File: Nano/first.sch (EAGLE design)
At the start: 17 parts, among them J2 455-1750-1-ND, J3 455-1750-1-ND

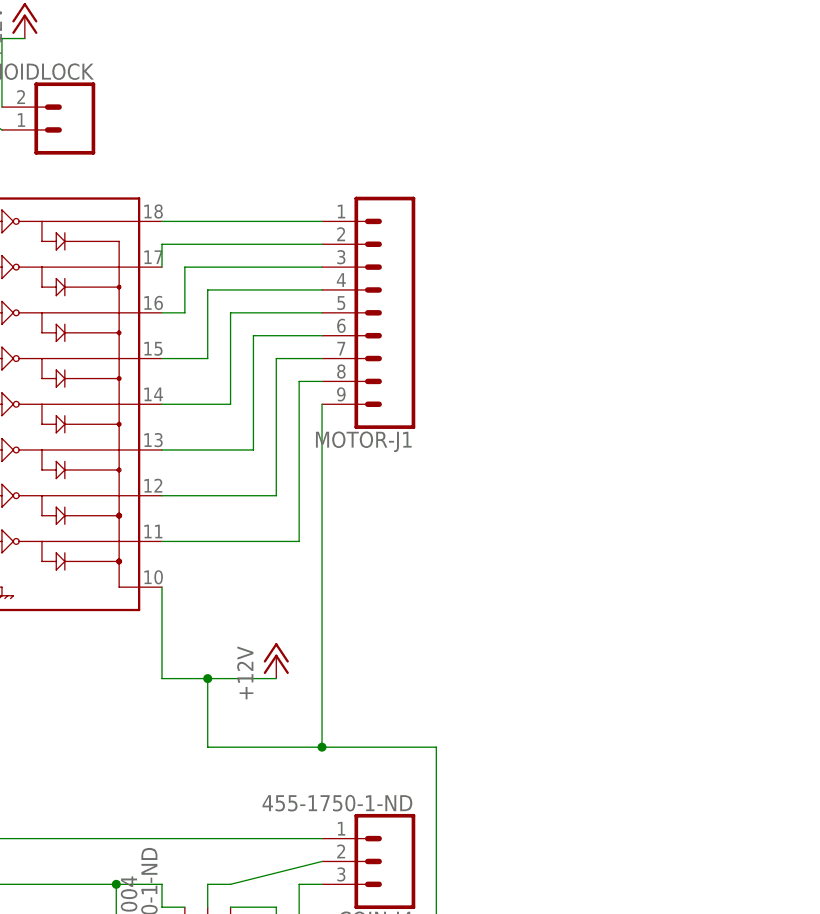
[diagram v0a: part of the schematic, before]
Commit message: Mini board schematic updated (molex conn added, uno mirrored, tracks and via changed)
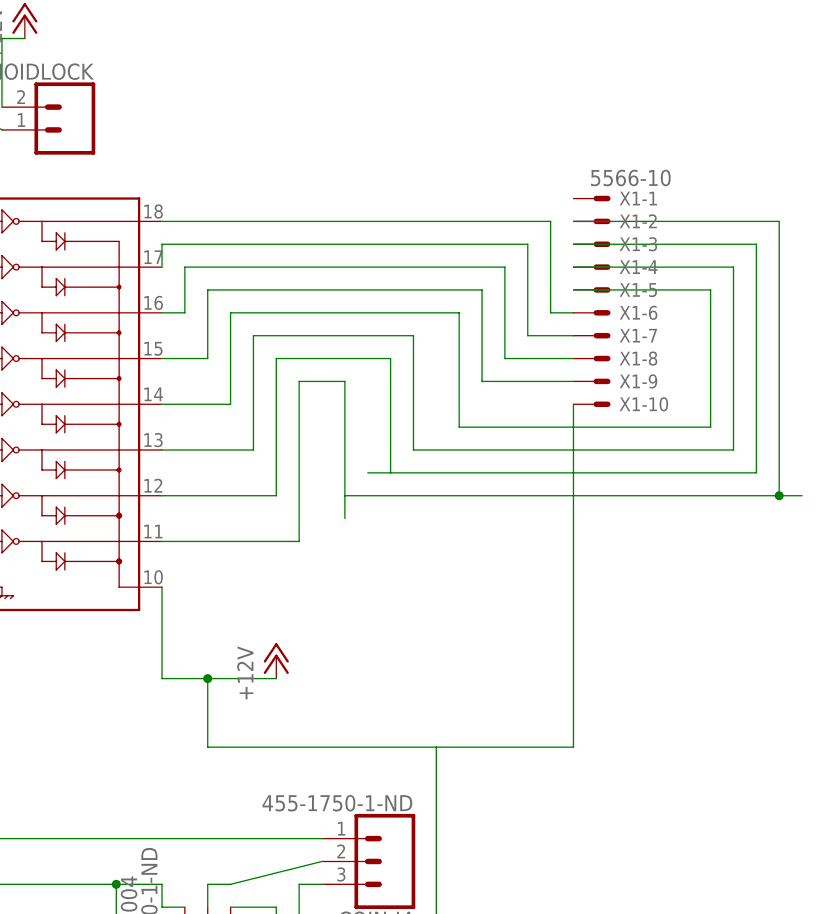
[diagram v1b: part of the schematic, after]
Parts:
- removed MOTOR-J1: (no value), wendor:CONN_09LONGPADS
- added X1: 5566-10, con-molex:5566-10
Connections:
- net +12V: now also X1-10.S; no longer MOTOR-J1.9
- net N$10: now also X1-7.S; no longer MOTOR-J1.2
- net N$11: now also X1-8.S; no longer MOTOR-J1.3
- net N$12: now also X1-9.S; no longer MOTOR-J1.4
- net N$13: now also X1-5.S; no longer MOTOR-J1.5
- net N$14: now also X1-4.S; no longer MOTOR-J1.6
- net N$15: now also X1-3.S; no longer MOTOR-J1.7
- net N$16: now also X1-2.S; no longer MOTOR-J1.8
- net N$9: now also X1-6.S; no longer MOTOR-J1.1
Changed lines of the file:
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@@
 <attribute name="OC_NEWARK" value="71M1030"/>
-</part>
-<part name="MOTOR-J1" library="wendor" deviceset="CONN_09" device="LONGPADS">
-<attribute name="MF" value=""/>
-<attribute name="MPN" value=""/>
-<attribute name="OC_NEWARK" value="unknown"/>
 </part>
 <part name="LAZER-J2" library="wendor" deviceset="CONN_02" device="">
@@
 <part name="J5" library="wendor" deviceset="CONN_06" device="LONGPADS"/>
 <part name="J6" library="wendor" deviceset="CONN_06" device="LONGPADS"/>
+<part name="X1" library="con-molex" library_urn="urn:adsk.eagle:library:165" deviceset="5566-10" device=""/>
 </parts>
 <sheets>
@@
 <attribute name="MF" x="45.72" y="38.1" size="1.778" layer="96" display="off"/>
 <attribute name="MPN" x="45.72" y="38.1" size="1.778" layer="96" display="off"/>
-</instance>
-<instance part="MOTOR-J1" gate="G$1" x="177.8" y="38.1" rot="R180">
-<attribute name="OC_NEWARK" x="177.8" y="38.1" size="1.778" layer="96" display="off"/>
-<attribute name="MF" x="177.8" y="38.1" size="1.778" layer="96" display="off"/>
-<attribute name="MPN" x="177.8" y="38.1" size="1.778" layer="96" display="off"/>
 </instance>
 <instance part="LAZER-J2" gate="G$1" x="45.72" y="10.16">
@@
 <instance part="J5" gate="G$1" x="-10.16" y="45.72"/>
 <instance part="J6" gate="G$1" x="-10.16" y="20.32"/>
+<instance part="X1" gate="-1" x="198.12" y="50.8"/>
+<instance part="X1" gate="-2" x="198.12" y="48.26"/>
+<instance part="X1" gate="-3" x="198.12" y="45.72"/>
+<instance part="X1" gate="-4" x="198.12" y="43.18"/>
+<instance part="X1" gate="-5" x="198.12" y="40.64"/>
+<instance part="X1" gate="-6" x="198.12" y="38.1"/>
+<instance part="X1" gate="-7" x="198.12" y="35.56"/>
+<instance part="X1" gate="-8" x="198.12" y="33.02"/>
+<instance part="X1" gate="-9" x="198.12" y="30.48"/>
+<instance part="X1" gate="-10" x="198.12" y="27.94"/>
 </instances>
 <busses>
@@
 <segment>
 <pinref part="ULN1" gate="G$1" pin="18"/>
-<pinref part="MOTOR-J1" gate="G$1" pin="1"/>
-<wire x1="149.86" y1="48.26" x2="167.64" y2="48.26" width="0.1524" layer="91"/>
+<wire x1="149.86" y1="48.26" x2="193.04" y2="48.26" width="0.1524" layer="91"/>
+<wire x1="193.04" y1="48.26" x2="193.04" y2="38.1" width="0.1524" layer="91"/>
+<pinref part="X1" gate="-6" pin="S"/>
+<wire x1="193.04" y1="38.1" x2="195.58" y2="38.1" width="0.1524" layer="91"/>
 </segment>
 </net>
@@
 <pinref part="ULN1" gate="G$1" pin="17"/>
 <wire x1="149.86" y1="43.18" x2="149.86" y2="45.72" width="0.1524" layer="91"/>
-<pinref part="MOTOR-J1" gate="G$1" pin="2"/>
-<wire x1="149.86" y1="45.72" x2="167.64" y2="45.72" width="0.1524" layer="91"/>
+<wire x1="149.86" y1="45.72" x2="190.5" y2="45.72" width="0.1524" layer="91"/>
+<wire x1="190.5" y1="45.72" x2="190.5" y2="35.56" width="0.1524" layer="91"/>
+<pinref part="X1" gate="-7" pin="S"/>
+<wire x1="190.5" y1="35.56" x2="195.58" y2="35.56" width="0.1524" layer="91"/>
 </segment>
 </net>
@@
 <wire x1="149.86" y1="38.1" x2="152.4" y2="38.1" width="0.1524" layer="91"/>
 <wire x1="152.4" y1="38.1" x2="152.4" y2="43.18" width="0.1524" layer="91"/>
-<pinref part="MOTOR-J1" gate="G$1" pin="3"/>
-<wire x1="152.4" y1="43.18" x2="167.64" y2="43.18" width="0.1524" layer="91"/>
+<wire x1="152.4" y1="43.18" x2="187.96" y2="43.18" width="0.1524" layer="91"/>
+<wire x1="187.96" y1="43.18" x2="187.96" y2="33.02" width="0.1524" layer="91"/>
+<pinref part="X1" gate="-8" pin="S"/>
+<wire x1="187.96" y1="33.02" x2="195.58" y2="33.02" width="0.1524" layer="91"/>
 </segment>
 </net>
@@
 <wire x1="149.86" y1="33.02" x2="154.94" y2="33.02" width="0.1524" layer="91"/>
 <wire x1="154.94" y1="33.02" x2="154.94" y2="40.64" width="0.1524" layer="91"/>
-<pinref part="MOTOR-J1" gate="G$1" pin="4"/>
-<wire x1="154.94" y1="40.64" x2="167.64" y2="40.64" width="0.1524" layer="91"/>
+<wire x1="154.94" y1="40.64" x2="185.42" y2="40.64" width="0.1524" layer="91"/>
+<wire x1="185.42" y1="40.64" x2="185.42" y2="30.48" width="0.1524" layer="91"/>
+<pinref part="X1" gate="-9" pin="S"/>
+<wire x1="185.42" y1="30.48" x2="195.58" y2="30.48" width="0.1524" layer="91"/>
 </segment>
 </net>
@@
 <wire x1="149.86" y1="27.94" x2="157.48" y2="27.94" width="0.1524" layer="91"/>
 <wire x1="157.48" y1="27.94" x2="157.48" y2="38.1" width="0.1524" layer="91"/>
-<pinref part="MOTOR-J1" gate="G$1" pin="5"/>
-<wire x1="157.48" y1="38.1" x2="167.64" y2="38.1" width="0.1524" layer="91"/>
+<wire x1="157.48" y1="38.1" x2="182.88" y2="38.1" width="0.1524" layer="91"/>
+<wire x1="182.88" y1="38.1" x2="182.88" y2="25.4" width="0.1524" layer="91"/>
+<wire x1="182.88" y1="25.4" x2="210.82" y2="25.4" width="0.1524" layer="91"/>
+<wire x1="210.82" y1="25.4" x2="210.82" y2="40.64" width="0.1524" layer="91"/>
+<pinref part="X1" gate="-5" pin="S"/>
+<wire x1="210.82" y1="40.64" x2="195.58" y2="40.64" width="0.1524" layer="91"/>
 </segment>
 </net>
@@
 <wire x1="149.86" y1="22.86" x2="160.02" y2="22.86" width="0.1524" layer="91"/>
 <wire x1="160.02" y1="22.86" x2="160.02" y2="35.56" width="0.1524" layer="91"/>
-<pinref part="MOTOR-J1" gate="G$1" pin="6"/>
-<wire x1="160.02" y1="35.56" x2="167.64" y2="35.56" width="0.1524" layer="91"/>
+<wire x1="160.02" y1="35.56" x2="177.8" y2="35.56" width="0.1524" layer="91"/>
+<wire x1="177.8" y1="35.56" x2="177.8" y2="22.86" width="0.1524" layer="91"/>
+<wire x1="177.8" y1="22.86" x2="213.36" y2="22.86" width="0.1524" layer="91"/>
+<wire x1="213.36" y1="22.86" x2="213.36" y2="43.18" width="0.1524" layer="91"/>
+<pinref part="X1" gate="-4" pin="S"/>
+<wire x1="213.36" y1="43.18" x2="195.58" y2="43.18" width="0.1524" layer="91"/>
 </segment>
 </net>
@@
 <pinref part="ULN1" gate="G$1" pin="12"/>
 <wire x1="162.56" y1="17.78" x2="149.86" y2="17.78" width="0.1524" layer="91"/>
-<pinref part="MOTOR-J1" gate="G$1" pin="7"/>
-<wire x1="167.64" y1="33.02" x2="162.56" y2="33.02" width="0.1524" layer="91"/>
 <wire x1="162.56" y1="33.02" x2="162.56" y2="17.78" width="0.1524" layer="91"/>
+<wire x1="162.56" y1="33.02" x2="175.26" y2="33.02" width="0.1524" layer="91"/>
+<wire x1="175.26" y1="33.02" x2="175.26" y2="20.32" width="0.1524" layer="91"/>
+<wire x1="175.26" y1="20.32" x2="172.72" y2="20.32" width="0.1524" layer="91"/>
+<wire x1="175.26" y1="20.32" x2="215.9" y2="20.32" width="0.1524" layer="91"/>
+<wire x1="215.9" y1="20.32" x2="215.9" y2="45.72" width="0.1524" layer="91"/>
+<pinref part="X1" gate="-3" pin="S"/>
+<wire x1="215.9" y1="45.72" x2="195.58" y2="45.72" width="0.1524" layer="91"/>
 </segment>
 </net>
@@
 <wire x1="149.86" y1="12.7" x2="165.1" y2="12.7" width="0.1524" layer="91"/>
 <wire x1="165.1" y1="12.7" x2="165.1" y2="30.48" width="0.1524" layer="91"/>
-<pinref part="MOTOR-J1" gate="G$1" pin="8"/>
-<wire x1="165.1" y1="30.48" x2="167.64" y2="30.48" width="0.1524" layer="91"/>
+<wire x1="165.1" y1="30.48" x2="170.18" y2="30.48" width="0.1524" layer="91"/>
+<wire x1="170.18" y1="30.48" x2="170.18" y2="17.78" width="0.1524" layer="91"/>
+<wire x1="170.18" y1="15.24" x2="170.18" y2="17.78" width="0.1524" layer="91"/>
+<wire x1="170.18" y1="17.78" x2="218.44" y2="17.78" width="0.1524" layer="91"/>
+<wire x1="220.98" y1="17.78" x2="218.44" y2="17.78" width="0.1524" layer="91"/>
+<wire x1="218.44" y1="17.78" x2="218.44" y2="48.26" width="0.1524" layer="91"/>
+<junction x="218.44" y="17.78"/>
+<pinref part="X1" gate="-2" pin="S"/>
+<wire x1="218.44" y1="48.26" x2="195.58" y2="48.26" width="0.1524" layer="91"/>
 </segment>
 </net>
@@
 <wire x1="149.86" y1="7.62" x2="149.86" y2="-2.54" width="0.1524" layer="91"/>
 <wire x1="149.86" y1="-2.54" x2="154.94" y2="-2.54" width="0.1524" layer="91"/>
-<pinref part="MOTOR-J1" gate="G$1" pin="9"/>
 <wire x1="154.94" y1="-2.54" x2="162.56" y2="-2.54" width="0.1524" layer="91"/>
-<wire x1="167.64" y1="27.94" x2="167.64" y2="-10.16" width="0.1524" layer="91"/>
-<wire x1="167.64" y1="-10.16" x2="154.94" y2="-10.16" width="0.1524" layer="91"/>
 <wire x1="154.94" y1="-10.16" x2="154.94" y2="-2.54" width="0.1524" layer="91"/>
 <junction x="154.94" y="-2.54"/>
-<wire x1="167.64" y1="-10.16" x2="180.34" y2="-10.16" width="0.1524" layer="91"/>
+<wire x1="154.94" y1="-10.16" x2="180.34" y2="-10.16" width="0.1524" layer="91"/>
 <wire x1="180.34" y1="-10.16" x2="180.34" y2="-33.02" width="0.1524" layer="91"/>
-<junction x="167.64" y="-10.16"/>
 <wire x1="180.34" y1="-33.02" x2="165.1" y2="-33.02" width="0.1524" layer="91"/>
 <wire x1="165.1" y1="-33.02" x2="165.1" y2="-25.4" width="0.1524" layer="91"/>
 <pinref part="COIN-J4" gate="J$1" pin="3"/>
 <wire x1="165.1" y1="-25.4" x2="167.64" y2="-25.4" width="0.1524" layer="91"/>
-</segment>
-<segment>
+<pinref part="X1" gate="-10" pin="S"/>
+<wire x1="180.34" y1="-10.16" x2="195.58" y2="-10.16" width="0.1524" layer="91"/>
+<wire x1="195.58" y1="-10.16" x2="195.58" y2="27.94" width="0.1524" layer="91"/>
+</segment>
+<segment>
